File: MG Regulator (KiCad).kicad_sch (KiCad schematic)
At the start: 17 parts, among them J1 10K thermistor connector, Q1 AM2336N-CT, T1 B+, T2 +, T3 -, T4 F, U1 AP7370-50FDC, U2 ACS723LLCTR-10AU-T

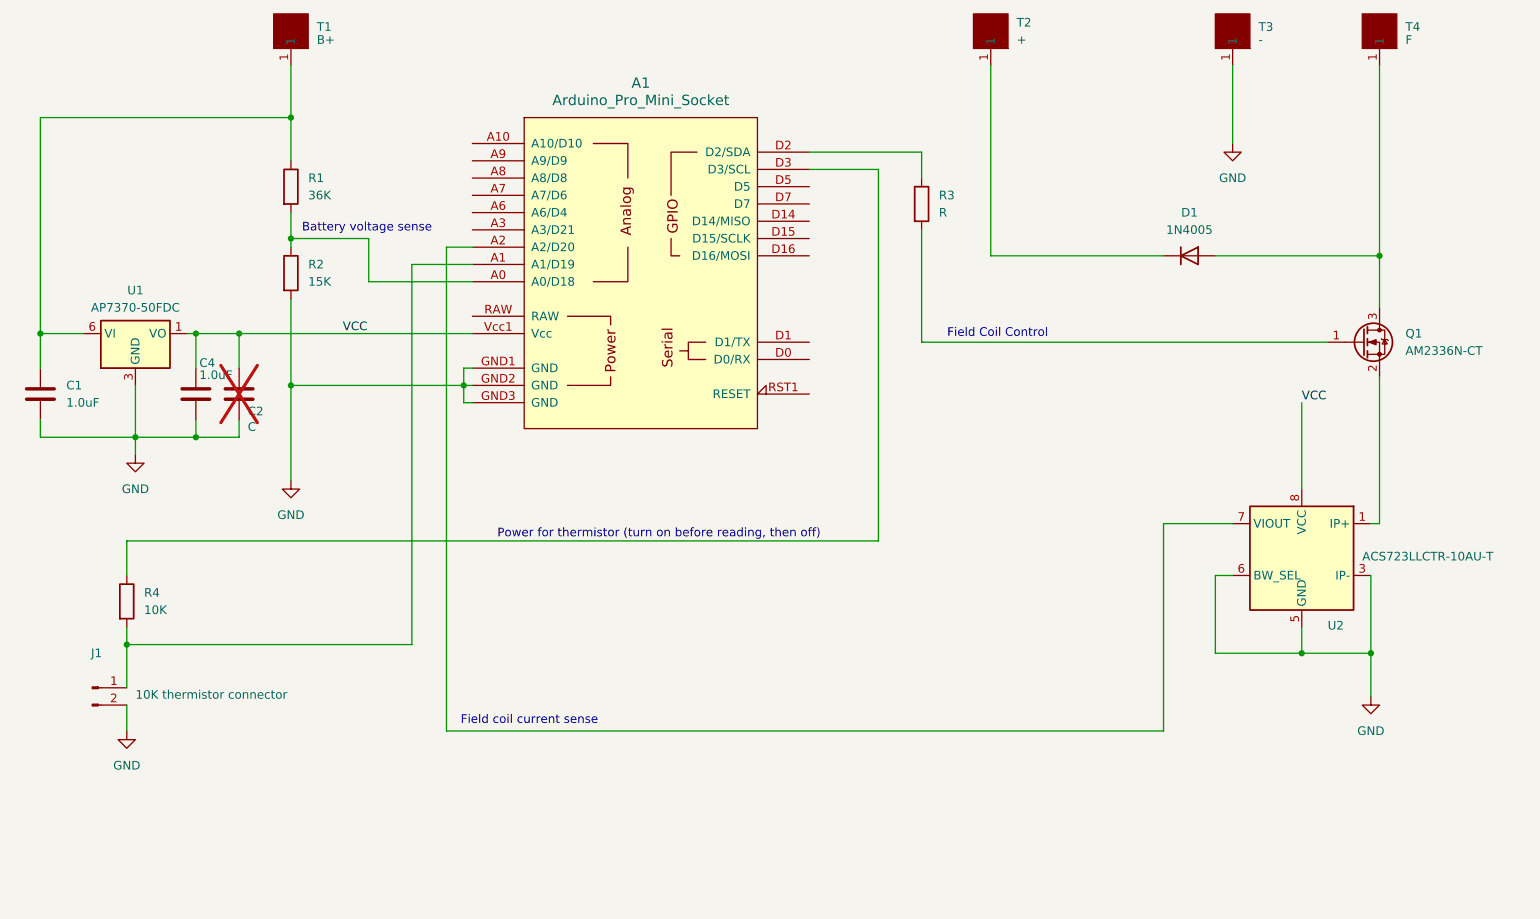
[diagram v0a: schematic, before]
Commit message: Lastest vesion with switch to turn on LED when ignition turns on.
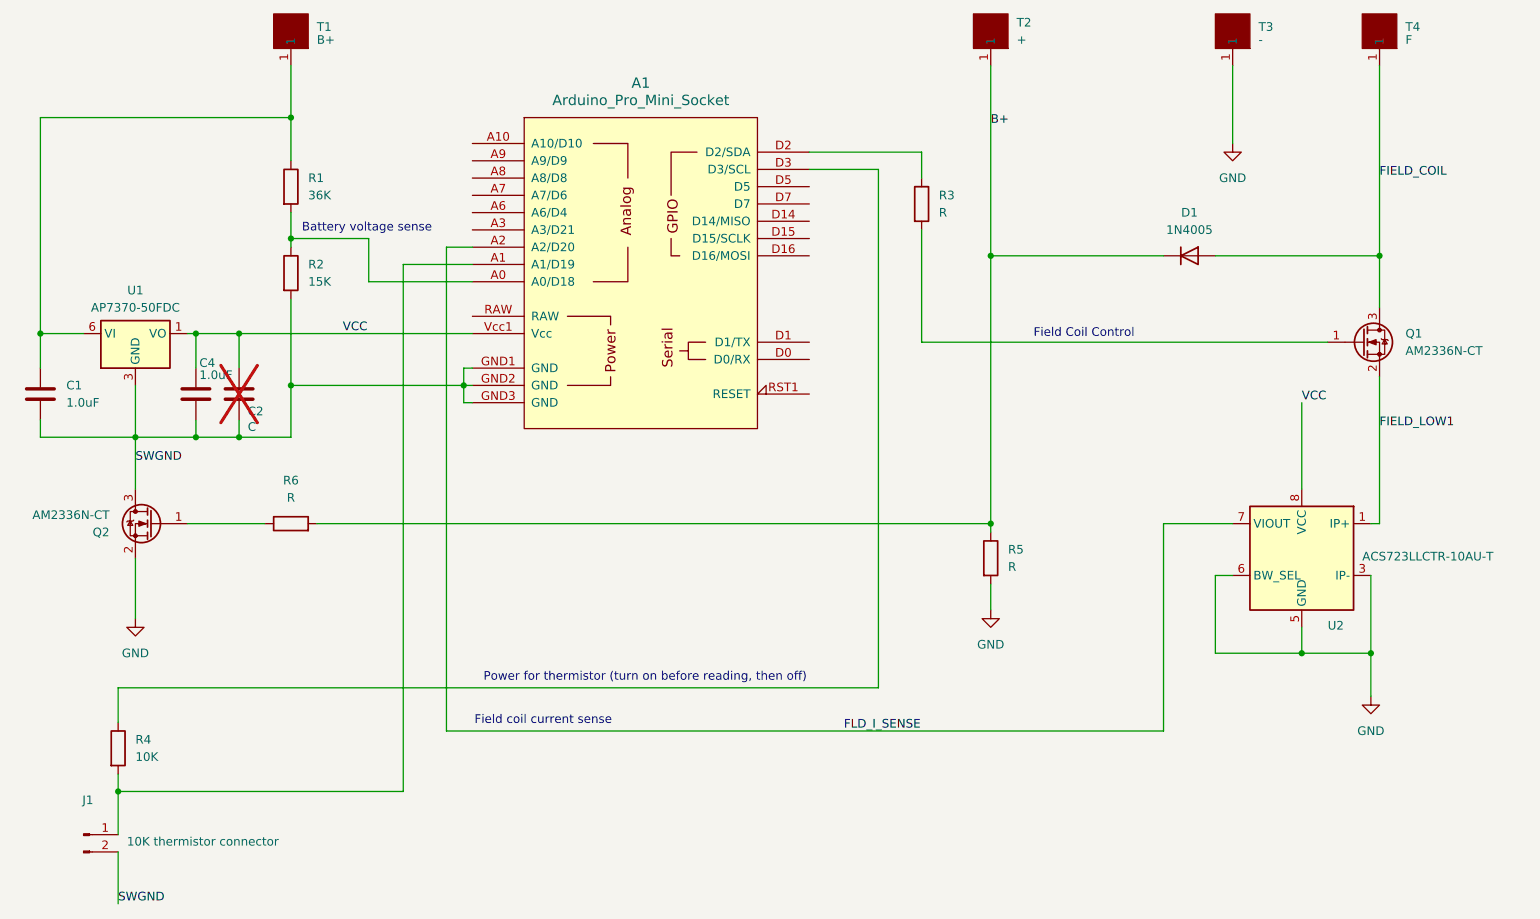
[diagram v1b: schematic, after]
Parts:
- added Q2: AM2336N-CT, Package_TO_SOT_SMD:TSOT-23, symbol Transistor_FET:IRLML2060
- added R5, R6: R, Resistor_SMD:R_0805_2012Metric, symbol Device:R
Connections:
- net GND: now also Q2.2 (S), R5.2; no longer A1.GND1 (GND), A1.GND2 (GND), A1.GND3 (GND), C1.2, C2.2, C4.2, J1.2 (Pin_2), R2.2, U1.3 (GND), U1.7 (GND)
- net FIELD_COIL: now reaches D1.2 (A), Q1.3 (D), T4.1
- net FLD_I_SENSE: now reaches A1.A2 (A2/D20), U2.7 (VIOUT)
- net B+: now reaches D1.1 (K), T2.1
- net B+: now also R5.1, R6.2
- net FIELD_LOW1: now reaches Q1.2 (S), U2.1 (IP+), U2.2 (IP+)
- new net: Q2.1 (G), R6.1
- new net SWGND: A1.GND1 (GND), A1.GND2 (GND), A1.GND3 (GND), C1.2, C2.2, C4.2, J1.2 (Pin_2), Q2.3 (D), R2.2, U1.3 (GND), U1.7 (GND)
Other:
- moved on the sheet: J1, R4
